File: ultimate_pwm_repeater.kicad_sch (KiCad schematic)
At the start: 21 parts, among them J1 POWER, J2 SIGNAL, Q1 IRF3205, Q2 IRF3205, Q3 IRF3205, Q4 IRF3205

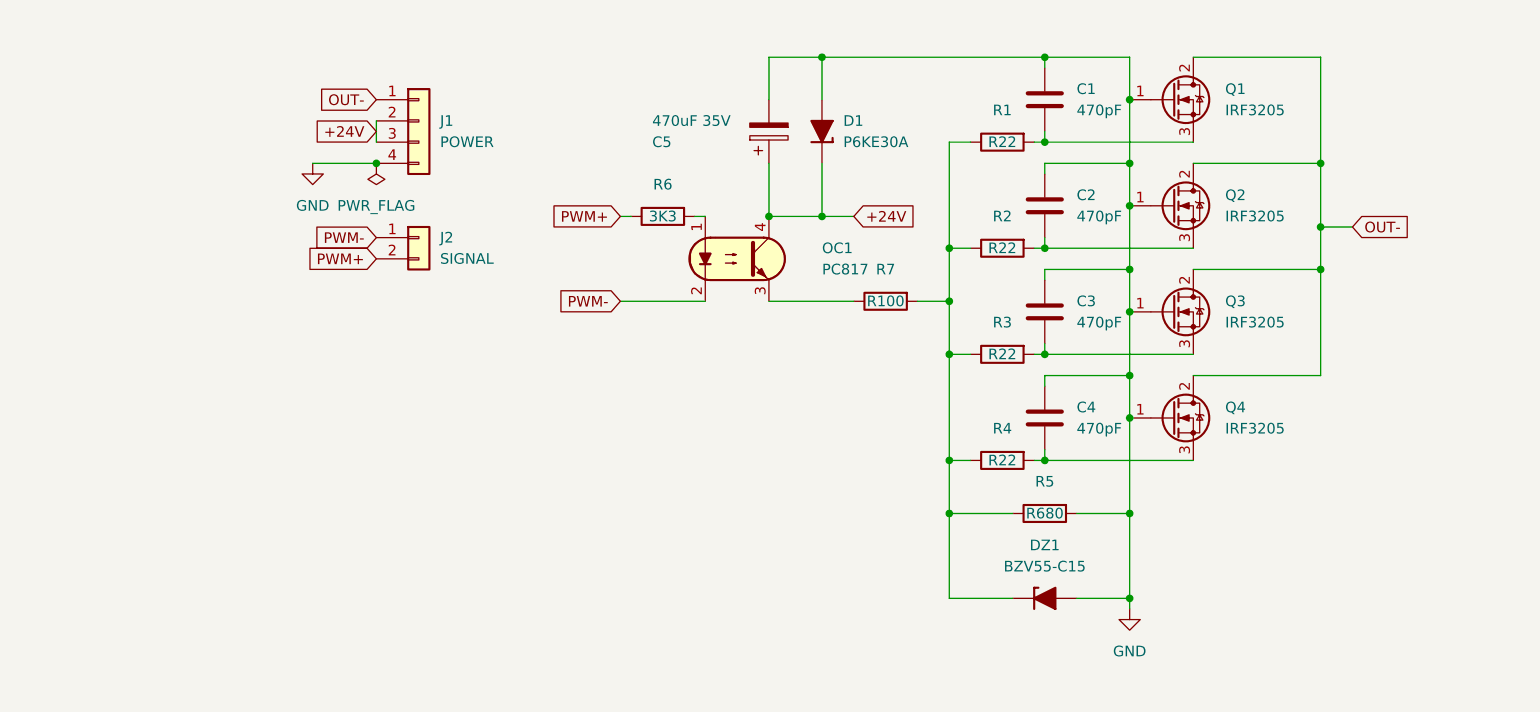
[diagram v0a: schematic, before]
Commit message: fixed reverse mosfet connection, rearranged pcb
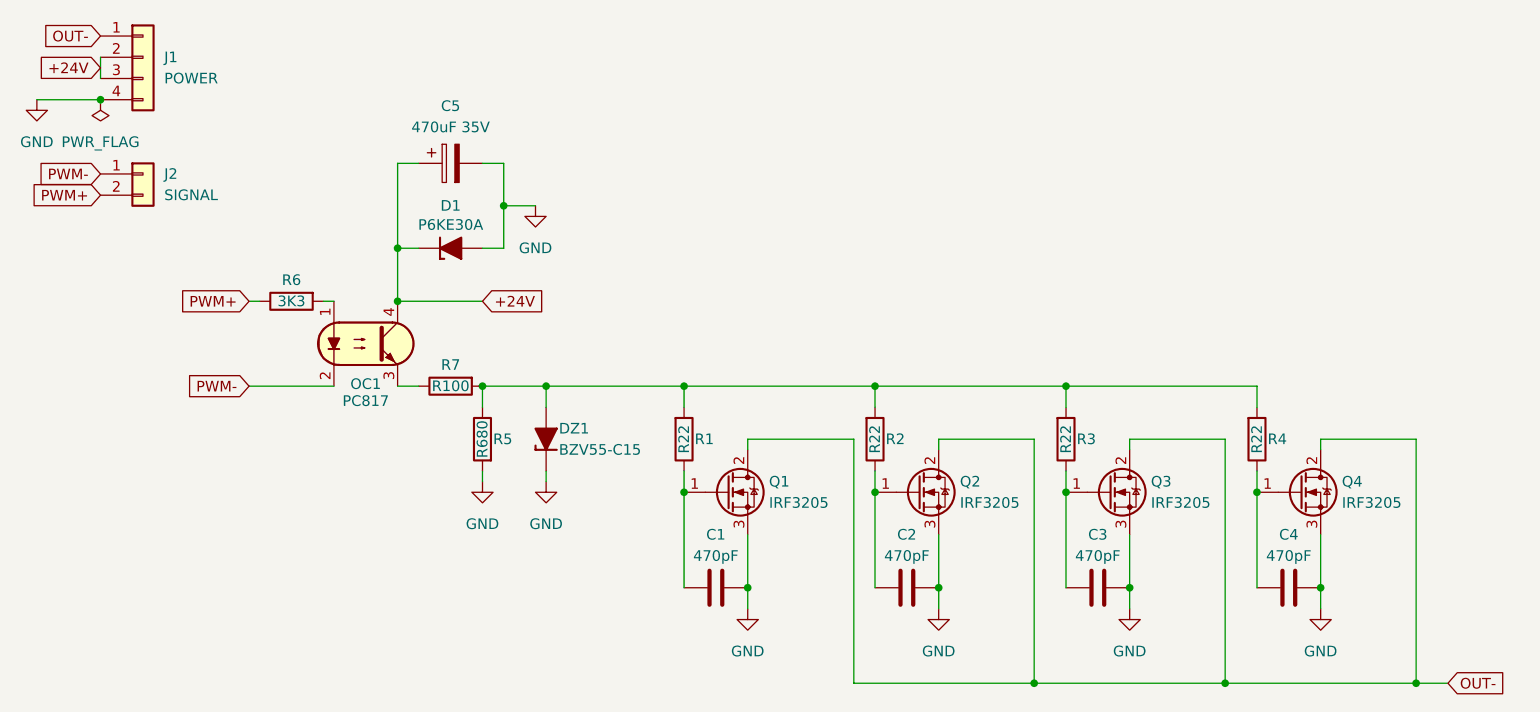
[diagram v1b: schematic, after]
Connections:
- net GND: now also C2.2, C4.2, DZ1.1 (K), Q1.3 (S), Q2.3 (S), Q3.3 (S), Q4.3 (S); no longer C2.1, C4.1, DZ1.2 (A), Q1.1 (G), Q2.1 (G), Q3.1 (G), Q4.1 (G)
- new net: DZ1.2 (A), R1.1, R2.1, R3.1, R4.1, R5.2, R7.1
- new net: C3.2, Q3.1 (G), R3.2
- new net: C1.2, Q1.1 (G), R1.2
- new net: C4.1, Q4.1 (G), R4.2
- new net: C2.1, Q2.1 (G), R2.2
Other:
- moved on the sheet: C1, C2, C3, C4, C5, D1, DZ1, J1, J2, OC1, Q1, Q2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

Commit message: 18v zener, 3.5mm pitch capacitor
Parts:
- C5: footprint PCM_Capacitor_THT_AKL:CP_Radial_D10.0mm_P2.50mm -> Capacitor_THT:CP_Radial_D10.0mm_P3.50mm; symbol PCM_Capacitor_AKL:CP_Radial_D10.0mm_P2.50mm -> PCM_Capacitor_AKL:CP_Radial_D10.0mm_P3.50mm
- DZ1: value BZV55-C15 -> BZV55-C18; symbol PCM_Diode_Zener_AKL:BZV55-C15 -> PCM_Diode_Zener_AKL:BZV55-C18
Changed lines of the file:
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@@
 	(title_block
 		(title "PWM Repeater")
-		(date "2025-05-09")
-		(rev "0.5")
+		(date "2025-06-10")
+		(rev "0.6")
 		(company "Hex of the River and the Sparks")
 	)
@@
 	)
 	(symbol
-		(lib_id "PCM_Capacitor_AKL:CP_Radial_D10.0mm_P2.50mm")
+		(lib_id "PCM_Capacitor_AKL:CP_Radial_D10.0mm_P3.50mm")
 		(at 67.31 35.56 90)
 		(mirror x)
@@
 			)
 		)
-		(property "Footprint" "PCM_Capacitor_THT_AKL:CP_Radial_D10.0mm_P2.50mm"
+		(property "Footprint" "Capacitor_THT:CP_Radial_D10.0mm_P3.50mm"
 			(at 77.47 35.56 0)
 			(effects
@@
 			)
 		)
-		(property "Description" "THT Electrolytic Capacitor, 10.0mm Diameter, 2.50mm Pitch, European Symbol, Alternate KiCad Library"
+		(property "Description" "THT Electrolytic Capacitor, 10.0mm Diameter, 3.50mm Pitch, European Symbol, Alternate KiCad Library"
 			(at 67.31 35.56 0)
 			(effects
@@
 	)
 	(symbol
-		(lib_id "PCM_Diode_Zener_AKL:BZV55-C15")
+		(lib_id "PCM_Diode_Zener_AKL:BZV55-C18")
 		(at 78.74 68.58 90)
 		(mirror x)
@@
 			)
 		)
-		(property "Value" "BZV55-C15"
+		(property "Value" "BZV55-C18"
 			(at 80.264 69.85 90)
 			(effects
@@
 			)
 		)
-		(property "Description" "MiniMELF Zener diode, 15V, 400mW, Alternate KiCAD Library"
+		(property "Description" "MiniMELF Zener diode, 18V, 400mW, Alternate KiCAD Library"
 			(at 78.74 68.58 0)
 			(effects
